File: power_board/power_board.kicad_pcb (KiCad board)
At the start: 4 copper layers, 46 x 60 mm, 53 parts, among them J1 USB-C receptacle (input from 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, J2 USB-C receptacle (5 V to Pi), J3 Lidar 15 V (pluggable 3.5 mm), J4 Latching 16 mm LED button (JS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, J5 To Pi GPIO (JST-PH 10), U1 CH224A, U3 TPS56637RPA, U4 TPS26631PWP, U5 INA226 (addr 0x40)

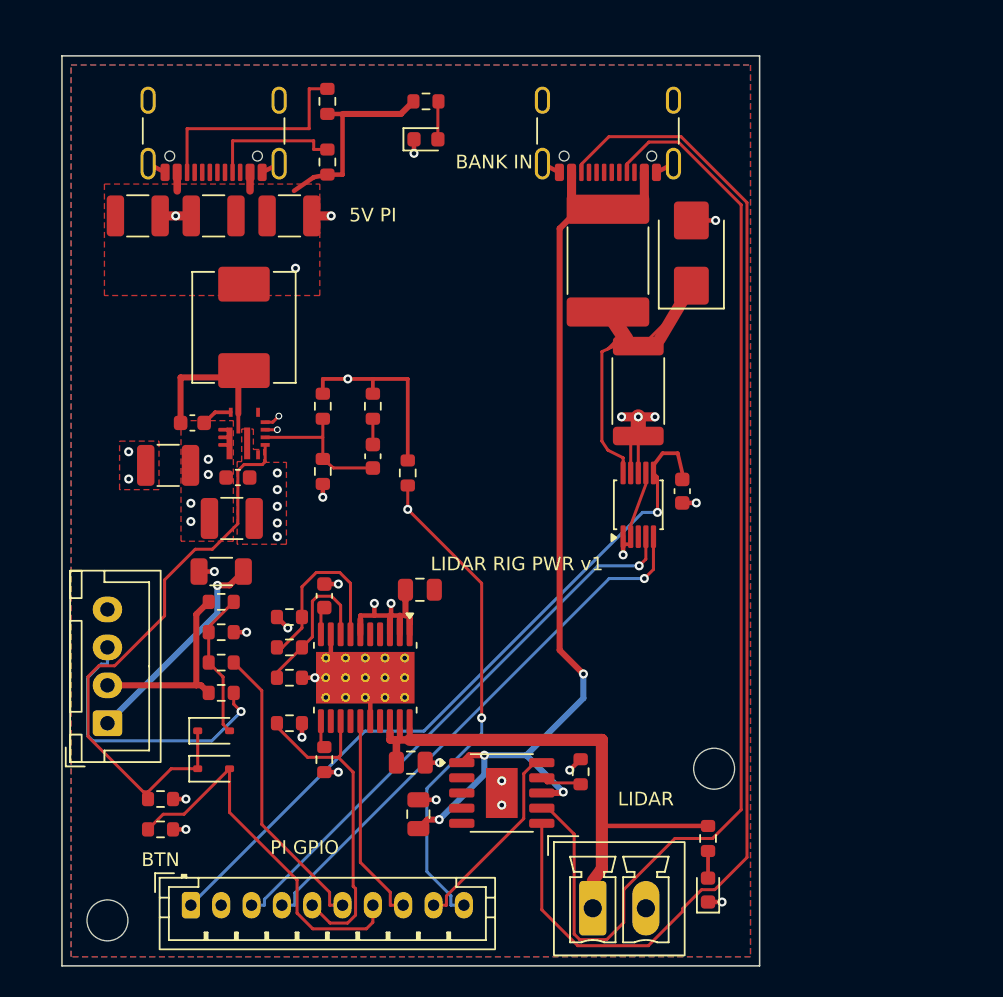
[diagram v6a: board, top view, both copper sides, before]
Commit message: Power board: HRO TYPE-C-31-M-12 sockets (in stock), KT-0603R/W Basic LEDs, FMF25 shunt; CC traces between the shell pads
Co-Authored-By: Claude Opus 5.5 <noreply@anthropic.com>
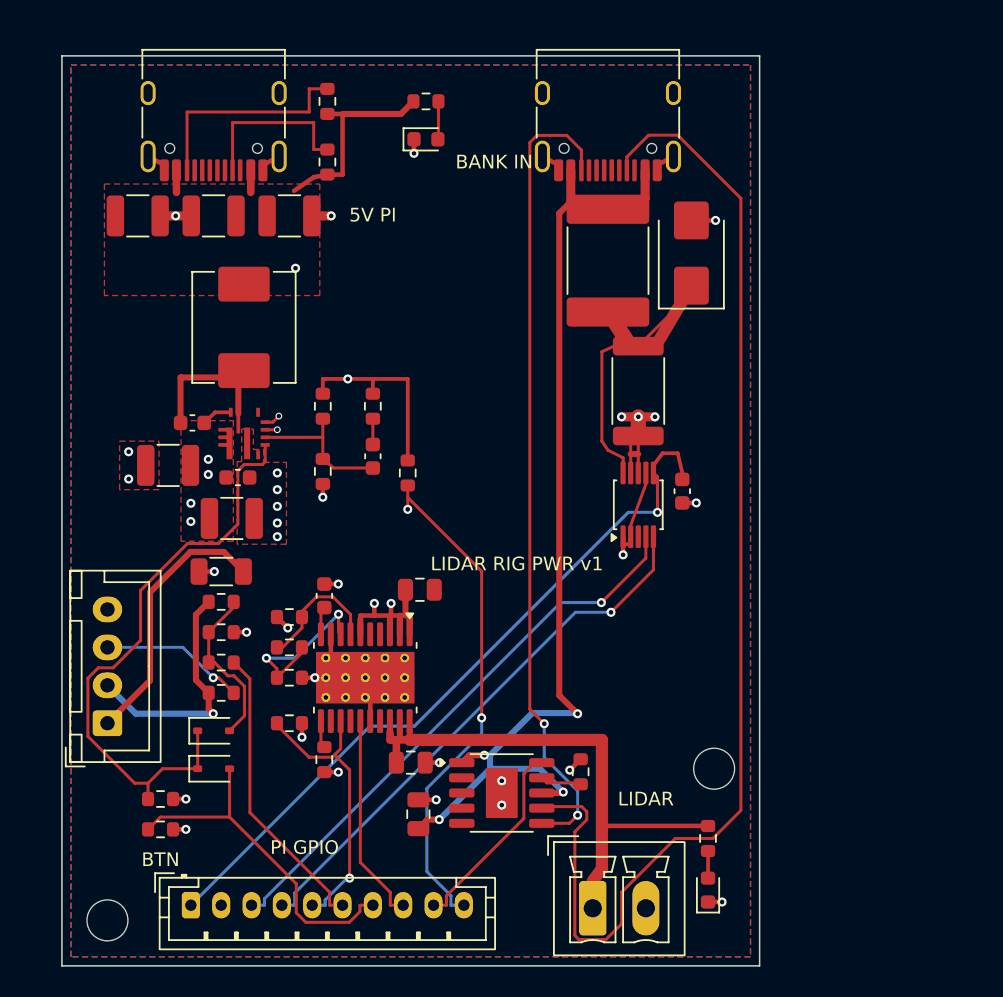
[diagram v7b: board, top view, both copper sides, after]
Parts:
- D2: value green -> red
- D3: value blue -> white
- J1, J2: footprint Connector_USB:USB_C_Receptacle_GCT_USB4105-xx-A_16P_TopMnt_Horizontal -> Connector_USB:USB_C_Receptacle_HRO_TYPE-C-31-M-12
- moved J1 0.50 mm to (36.0, 3.50)
- moved J2 0.50 mm to (10.0, 3.50)
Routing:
- net /IN_CC2: track 79.9 -> 53.6 mm, vias 0 -> 2
- net /BTN_LED_A: track 19.1 -> 9.57 mm
- net /EF_UVLO: track 12.1 -> 8.66 mm
- net /SW_FEED: track 14.2 -> 17.6 mm, vias 1 -> 0
- net /SW_ON: track 12.7 -> 15.9 mm, vias 0 -> 1
- net /VBUS_RAW: track 65.3 -> 68.3 mm
- net /IN_CC1: track 75.7 -> 78.5 mm
- net /LIDAR_EN: track 22.0 -> 19.2 mm, vias 0 -> 1
- net /OUT_CC1: track 8.90 -> 11.2 mm
- net /KEEP_ALIVE: track 25.1 -> 23.1 mm
- net /EF_OVP: track 10.2 -> 11.6 mm, vias 0 -> 2
- net /SW_TAP: track 9.75 -> 11.0 mm
- net /VIN15: track 21.3 -> 22.4 mm
- net /BUCK_PG: track 48.4 -> 49.2 mm
- net /BUCK_EN: track 38.4 -> 39.0 mm
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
